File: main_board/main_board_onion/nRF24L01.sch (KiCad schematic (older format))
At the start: 20 parts, among them Q8 BSS138, U10 nRF24L01P, U11 molex_antenna_47948-0001, U9 Trinket_M0, Y2 16Mhz

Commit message: Forgot to save before last commit
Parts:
- removed Q8: BSS138, Package_TO_SOT_SMD:SOT-23, symbol Transistor_FET:BSS138
- removed U9: Trinket_M0, Trinket:Trinket_M0_noMounting, symbol Trinket:Trinket_M0
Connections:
- net labels removed: 5V, Trinket_RST
- wire segments 88 -> 75
- no-connect marks 5 -> 4
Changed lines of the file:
@@
 $Descr A4 11693 8268
 encoding utf-8
-Sheet 6 6
+Sheet 6 7
 Title ""
 Date ""
@@
 Wire Wire Line
 	7525 2050 7425 2050
-Text HLabel 2075 3725 0    50   Input ~ 0
-5V
 Connection ~ 6075 1100
 Wire Wire Line
@@
 Text Label 6525 775  2    50   ~ 0
 3v3_Trinket
-$Comp
-L Trinket:Trinket_M0 U9
-U 1 1 5D093872
-P 3075 3925
-AR Path="/5D093872" Ref="U9"  Part="1"
-AR Path="/5D07F3D0/5D093872" Ref="U9"  Part="1"
-F 0 "U9" H 3025 4390 50  0000 C CNN
-F 1 "Trinket_M0" H 3025 4299 50  0000 C CNN
-F 2 "Trinket:Trinket_M0_noMounting" H 3025 4025 50  0001 C CNN
-F 3 "https://learn.adafruit.com/adafruit-trinket-m0-circuitpython-arduino/downloads" H 3025 4025 50  0001 C CNN
-	1    3075 3925
-	1    0    0    -1
-$EndComp
-NoConn ~ 3775 3725
-$Comp
-L Transistor_FET:BSS138 Q8
-U 1 1 5D099668
-P 1975 4525
-F 0 "Q8" V 2226 4525 50  0000 C CNN
-F 1 "BSS138" V 2317 4525 50  0000 C CNN
-F 2 "Package_TO_SOT_SMD:SOT-23" H 2175 4450 50  0001 L CIN
-F 3 "https://www.fairchildsemi.com/datasheets/BS/BSS138.pdf" H 1975 4525 50  0001 L CNN
-	1    1975 4525
-	1    0    0    -1
-$EndComp
-Wire Wire Line
-	2275 4125 2075 4125
-Wire Wire Line
-	2075 4125 2075 4325
-Wire Wire Line
-	2075 4725 2075 4875
-Wire Wire Line
-	2075 4875 2275 4875
-Text Label 2275 4875 2    50   ~ 0
-GND
-Text Label 1750 4525 2    50   ~ 0
-Trinket_RST
-Wire Wire Line
-	1775 4525 1325 4525
-Text HLabel 1325 4525 0    50   Input ~ 0
-Trinket_RST
-Text Label 2100 3825 0    50   ~ 0
-GND
-Wire Wire Line
-	2100 3825 2275 3825
-Text Label 4250 4125 2    50   ~ 0
-3v3_Trinket
 NoConn ~ 6825 3000
 Text Label 6775 2900 2    50   ~ 0
 nRF_CE
-Text Label 1900 4025 0    50   ~ 0
-nRF_SCK
-Text Label 4125 3925 2    50   ~ 0
-nRF_CSN
-Text Label 4075 3825 2    50   ~ 0
-nRF_CE
-Text Label 1875 3925 0    50   ~ 0
-nRF_MOSI
-Text Label 4175 4025 2    50   ~ 0
-nRF_MISO
 Wire Wire Line
 	6400 2500 6825 2500
@@
 	6400 2900 6825 2900
 Wire Wire Line
-	3775 3925 4125 3925
-Wire Wire Line
-	3775 3825 4075 3825
-Wire Wire Line
-	2275 3925 1875 3925
-Wire Wire Line
-	3775 4025 4175 4025
-Wire Wire Line
-	2275 4025 1900 4025
-Wire Wire Line
-	2075 3725 2275 3725
-Wire Wire Line
-	3775 4125 4250 4125
-Wire Wire Line
 	6075 775  6525 775
 Wire Wire Line
 	6775 2050 7325 2050
+$Sheet
+S 2975 3225 1900 1400
+U 5D0BDDAB
+F0 "Trinket_M0_rev_D" 50
+F1 "/home/jonathan/Projects/SB_CAD/SUPERball/superball_v2_electronics/Adafruit-Trinket-M0-PCB-master/Trinket M0 rev D/Trinket_M0_rev_D.sch" 50
+$EndSheet
 $EndSCHEMATC

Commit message: pulled updated sch files from dev_nRF24 branch. Need to get new nRF24 lib from same branch.
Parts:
- removed C33: 1nF, Capacitor_SMD:C_0603_1608Metric, symbol Device:C_Small
- U10: symbol RF:nRF24L01P -> New_nRF24:nRF24L01P
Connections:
- net labels added: 3v3, Trinket_RESET
- wire segments 75 -> 84
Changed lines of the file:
@@
 EESchema Schematic File Version 5
-LIBS:main_board_onion-cache
+LIBS:nRF24_testing-cache
 EELAYER 29 0
 EELAYER END
 $Descr A4 11693 8268
 encoding utf-8
-Sheet 6 7
+Sheet 2 3
 Title ""
 Date ""
@@
 Wire Wire Line
 	6075 825  6075 775
-Connection ~ 7425 3775
 Wire Wire Line
 	5900 775  6075 775
@@
 	1    0    0    -1
 $EndComp
-Text Label 6775 2700 2    50   ~ 0
-nRF_CSN
 Wire Wire Line
 	8325 3850 8275 3850
@@
 Wire Wire Line
 	8275 3500 8275 3850
-Wire Wire Line
-	5900 1100 5800 1100
 Text Label 8650 3675 2    50   ~ 0
 GND
 Wire Wire Line
 	8275 3400 8275 3500
-Text Label 7050 3775 0    50   ~ 0
-GND
 Wire Wire Line
 	5900 1025 5900 1100
@@
 	9475 2150 9475 2025
 Connection ~ 7325 2050
-Connection ~ 7325 3775
 Connection ~ 6075 775
 Text HLabel 6400 2600 0    50   Input ~ 0
@@
 Wire Wire Line
 	7425 2100 7425 2050
-Connection ~ 5900 1100
 Wire Wire Line
 	6075 1025 6075 1100
@@
 Text Label 6250 1100 2    50   ~ 0
 GND
-$Comp
-L Device:C_Small C33
-U 1 1 5D08136B
-P 6075 925
-F 0 "C33" H 6167 971 50  0000 L CNN
-F 1 "1nF" H 6167 880 50  0000 L CNN
-F 2 "Capacitor_SMD:C_0603_1608Metric" H 6075 925 50  0001 C CNN
-F 3 "~" H 6075 925 50  0001 C CNN
-	1    6075 925
-	1    0    0    -1
-$EndComp
 Wire Wire Line
 	5900 825  5900 775
-Text HLabel 5800 1100 0    50   Input ~ 0
+Text HLabel 1750 3900 0    50   Input ~ 0
 GND
 Wire Wire Line
@@
 Text Label 6775 2400 2    50   ~ 0
 nRF_MOSI
-Wire Wire Line
-	7425 3775 7325 3775
 Text HLabel 6400 2500 0    50   Input ~ 0
 nRF_MISO
 $Comp
-L RF:nRF24L01P U10
+L New_nRF24:nRF24L01P U10
 U 1 1 5D07F55C
 P 7425 2900
@@
 	0    -1   -1   0
 $EndComp
-Text Label 7050 3775 0    50   ~ 0
+Text Label 6975 3775 0    50   ~ 0
 GND
 Wire Wire Line
@@
 Text Label 8650 3350 2    50   ~ 0
 GND
-$Comp
-L Device:C_Small C37
-U 1 1 5D095A49
-P 8675 4075
-F 0 "C37" H 8767 4121 50  0000 L CNN
-F 1 "12pF" H 8767 4030 50  0000 L CNN
-F 2 "Capacitor_SMD:C_0603_1608Metric" H 8675 4075 50  0001 C CNN
-F 3 "~" H 8675 4075 50  0001 C CNN
-	1    8675 4075
-	1    0    0    -1
-$EndComp
 Wire Wire Line
 	9525 2825 10225 2825
@@
 $EndComp
 Wire Wire Line
-	6725 3775 7325 3775
+	6725 3775 7225 3775
 Connection ~ 8300 2600
 NoConn ~ 10925 2725
@@
 	6400 2600 6825 2600
 Wire Wire Line
-	6400 2700 6825 2700
-Wire Wire Line
 	6400 2900 6825 2900
 Wire Wire Line
@@
 	6775 2050 7325 2050
 $Sheet
-S 2975 3225 1900 1400
+S 1975 3550 1900 1400
 U 5D0BDDAB
 F0 "Trinket_M0_rev_D" 50
 F1 "/home/jonathan/Projects/SB_CAD/SUPERball/superball_v2_electronics/Adafruit-Trinket-M0-PCB-master/Trinket M0 rev D/Trinket_M0_rev_D.sch" 50
+F2 "3v3" I L 1975 3800 50
+F3 "GND" I L 1975 3900 50
+F4 "~RESET_M0" I L 1975 4200 50
+F5 "MISO" I R 3875 3775 50
+F6 "SCK" I R 3875 3875 50
+F7 "MOSI" I R 3875 3675 50
+F8 "D0{slash}CE" I R 3875 4175 50
+F9 "D1{slash}CSN" I R 3875 3975 50
 $EndSheet
+Text Label 6775 2700 2    50   ~ 0
+nRF_CSN
+Wire Wire Line
+	6400 2700 6825 2700
+Wire Wire Line
+	3875 3675 4300 3675
+Text Label 4250 3875 2    50   ~ 0
+nRF_SCK
+Text Label 4250 3775 2    50   ~ 0
+nRF_MISO
+Text Label 4250 4175 2    50   ~ 0
+nRF_CE
+Wire Wire Line
+	3875 4175 4300 4175
+Text Label 4250 3975 2    50   ~ 0
+nRF_CSN
+Wire Wire Line
+	3875 3775 4300 3775
+Wire Wire Line
+	3875 3975 4250 3975
+Text Label 4250 3675 2    50   ~ 0
+nRF_MOSI
+Wire Wire Line
+	3875 3875 4300 3875
+Text Label 1750 3900 0    50   ~ 0
+GND
+Wire Wire Line
+	1975 3900 1750 3900
+Text Label 1500 3800 0    50   ~ 0
+3v3_Trinket
+Wire Wire Line
+	1975 3800 1500 3800
+Wire Wire Line
+	1975 4200 1625 4200
+Text HLabel 1625 4200 0    50   Input ~ 0
+Trinket_RESET
+Text HLabel 1500 3800 0    50   Input ~ 0
+3v3
+$Comp
+L Device:C_Small C37
+U 1 1 5D095A49
+P 8675 4075
+F 0 "C37" H 8767 4121 50  0000 L CNN
+F 1 "12pF" H 8767 4030 50  0000 L CNN
+F 2 "Capacitor_SMD:C_0603_1608Metric" H 8675 4075 50  0001 C CNN
+F 3 "~" H 8675 4075 50  0001 C CNN
+	1    8675 4075
+	1    0    0    -1
+$EndComp
+Connection ~ 7325 3775
+Connection ~ 7425 3775
+Wire Wire Line
+	7425 3775 7325 3775
+Wire Wire Line
+	7225 3700 7225 3775
+Connection ~ 7225 3775
+Wire Wire Line
+	7225 3775 7325 3775
 $EndSCHEMATC

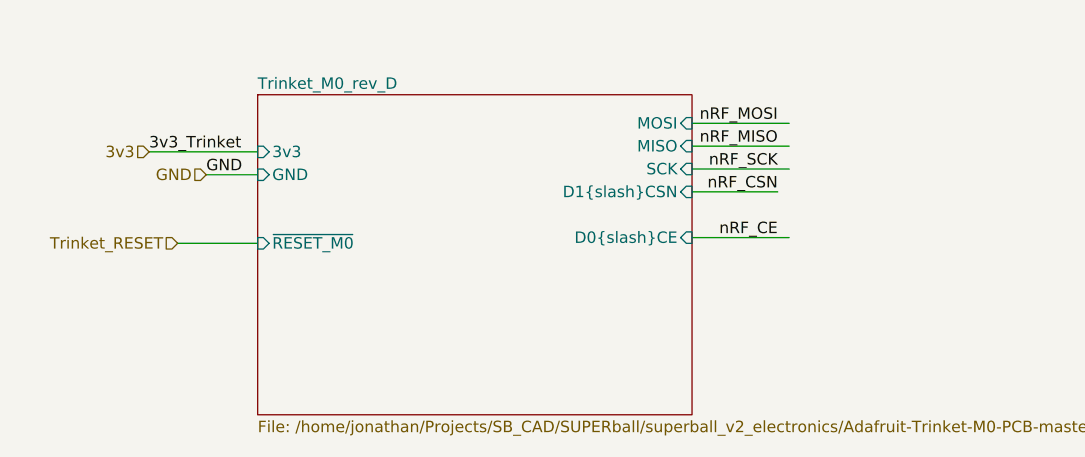
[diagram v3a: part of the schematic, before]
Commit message: Added new nRF24 library
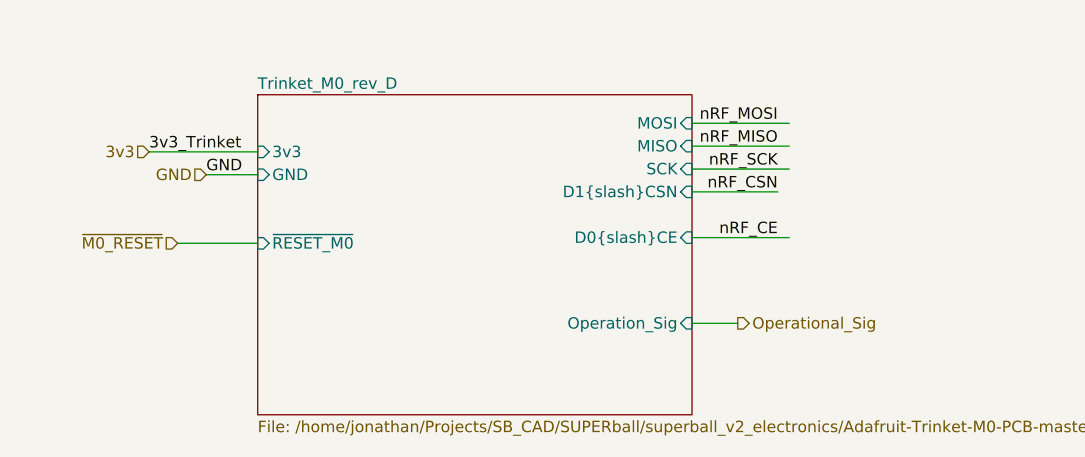
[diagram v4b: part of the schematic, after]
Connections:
- net labels added: Operational_Sig, ~M0_RESET
- net labels removed: Trinket_RESET
- wire segments 84 -> 85
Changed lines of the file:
@@
 EESchema Schematic File Version 5
-LIBS:nRF24_testing-cache
+LIBS:main_board_onion-cache
 EELAYER 29 0
 EELAYER END
 $Descr A4 11693 8268
 encoding utf-8
-Sheet 2 3
+Sheet 6 7
 Title ""
 Date ""
@@
 F8 "D0{slash}CE" I R 3875 4175 50
 F9 "D1{slash}CSN" I R 3875 3975 50
+F10 "Operation_Sig" I R 3875 4550 50
 $EndSheet
 Text Label 6775 2700 2    50   ~ 0
@@
 	1975 4200 1625 4200
 Text HLabel 1625 4200 0    50   Input ~ 0
-Trinket_RESET
+~M0_RESET
 Text HLabel 1500 3800 0    50   Input ~ 0
 3v3
@@
 Wire Wire Line
 	7225 3775 7325 3775
+Text HLabel 4075 4550 2    50   Output ~ 0
+Operational_Sig
+Wire Wire Line
+	3875 4550 4075 4550
 $EndSCHEMATC

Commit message: Finished initial routing of this design
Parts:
- C32, C34, C35, C36, C37, C38, C39, C40, C41: footprint Capacitor_SMD:C_0603_1608Metric -> Capacitor_SMD:C_0402_1005Metric
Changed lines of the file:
@@
 $Descr A4 11693 8268
 encoding utf-8
-Sheet 6 7
+Sheet 5 7
 Title ""
 Date ""
@@
 F 0 "C34" H 6167 971 50  0000 L CNN
 F 1 "1nF" H 6167 880 50  0000 L CNN
-F 2 "Capacitor_SMD:C_0603_1608Metric" H 6075 925 50  0001 C CNN
+F 2 "Capacitor_SMD:C_0402_1005Metric" H 6075 925 50  0001 C CNN
 F 3 "~" H 6075 925 50  0001 C CNN
 	1    6075 925
@@
 F 0 "C32" H 5700 1000 50  0000 L CNN
 F 1 "10nF" H 5650 875 50  0000 L CNN
-F 2 "Capacitor_SMD:C_0603_1608Metric" H 5900 925 50  0001 C CNN
+F 2 "Capacitor_SMD:C_0402_1005Metric" H 5900 925 50  0001 C CNN
 F 3 "~" H 5900 925 50  0001 C CNN
 	1    5900 925
@@
 F 0 "C36" H 8367 4121 50  0000 L CNN
 F 1 "12pF" H 8367 4030 50  0000 L CNN
-F 2 "Capacitor_SMD:C_0603_1608Metric" H 8275 4075 50  0001 C CNN
+F 2 "Capacitor_SMD:C_0402_1005Metric" H 8275 4075 50  0001 C CNN
 F 3 "~" H 8275 4075 50  0001 C CNN
 	1    8275 4075
@@
 F 0 "C35" H 6817 3646 50  0000 L CNN
 F 1 "33nF" H 6817 3555 50  0000 L CNN
-F 2 "Capacitor_SMD:C_0603_1608Metric" H 6725 3600 50  0001 C CNN
+F 2 "Capacitor_SMD:C_0402_1005Metric" H 6725 3600 50  0001 C CNN
 F 3 "~" H 6725 3600 50  0001 C CNN
 	1    6725 3600
@@
 F 0 "C40" V 9246 2250 50  0000 C CNN
 F 1 "4.7pF" V 9337 2250 50  0000 C CNN
-F 2 "Capacitor_SMD:C_0603_1608Metric" H 9475 2250 50  0001 C CNN
+F 2 "Capacitor_SMD:C_0402_1005Metric" H 9475 2250 50  0001 C CNN
 F 3 "~" H 9475 2250 50  0001 C CNN
 	1    9475 2250
@@
 F 0 "C39" V 8946 2825 50  0000 C CNN
 F 1 "1.5pF" V 9037 2825 50  0000 C CNN
-F 2 "Capacitor_SMD:C_0603_1608Metric" H 9175 2825 50  0001 C CNN
+F 2 "Capacitor_SMD:C_0402_1005Metric" H 9175 2825 50  0001 C CNN
 F 3 "~" H 9175 2825 50  0001 C CNN
 	1    9175 2825
@@
 Wire Wire Line
 	8025 2400 9125 2400
-$Comp
-L Device:C_Small C38
-U 1 1 5D0A7690
-P 9125 2250
-F 0 "C38" V 8896 2250 50  0000 C CNN
-F 1 "2.2nF" V 8987 2250 50  0000 C CNN
-F 2 "Capacitor_SMD:C_0603_1608Metric" H 9125 2250 50  0001 C CNN
-F 3 "~" H 9125 2250 50  0001 C CNN
-	1    9125 2250
-	-1   0    0    1
-$EndComp
 Wire Wire Line
 	8900 2825 9075 2825
@@
 F 0 "C41" V 9296 2950 50  0000 C CNN
 F 1 "1.0pF" V 9387 2950 50  0000 C CNN
-F 2 "Capacitor_SMD:C_0603_1608Metric" H 9525 2950 50  0001 C CNN
+F 2 "Capacitor_SMD:C_0402_1005Metric" H 9525 2950 50  0001 C CNN
 F 3 "~" H 9525 2950 50  0001 C CNN
 	1    9525 2950
@@
 F 0 "C37" H 8767 4121 50  0000 L CNN
 F 1 "12pF" H 8767 4030 50  0000 L CNN
-F 2 "Capacitor_SMD:C_0603_1608Metric" H 8675 4075 50  0001 C CNN
+F 2 "Capacitor_SMD:C_0402_1005Metric" H 8675 4075 50  0001 C CNN
 F 3 "~" H 8675 4075 50  0001 C CNN
 	1    8675 4075
@@
 Wire Wire Line
 	3875 4550 4075 4550
+$Comp
+L Device:C_Small C38
+U 1 1 5D0A7690
+P 9125 2250
+F 0 "C38" V 8896 2250 50  0000 C CNN
+F 1 "2.2nF" V 8987 2250 50  0000 C CNN
+F 2 "Capacitor_SMD:C_0402_1005Metric" H 9125 2250 50  0001 C CNN
+F 3 "~" H 9125 2250 50  0001 C CNN
+	1    9125 2250
+	-1   0    0    1
+$EndComp
 $EndSCHEMATC

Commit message: Added Gerber files for the version uploaded to MacroFab for manufacturing. Plus small changes made before uploading it.
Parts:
- Y2: value 16Mhz -> CX3225SB16000H0FLJCC
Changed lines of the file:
@@
 P 8475 3500
 F 0 "Y2" H 8331 3454 50  0000 R CNN
-F 1 "16Mhz" H 8331 3545 50  0000 R CNN
+F 1 " CX3225SB16000H0FLJCC " H 8331 3545 50  0000 R CNN
 F 2 "Crystal:Crystal_SMD_3225-4Pin_3.2x2.5mm" H 8475 3500 50  0001 C CNN
 F 3 "https://media.digikey.com/pdf/Data%20Sheets/AVX%20PDFs/CX3225SB_UKY1C-H1-16357-00_Spec.pdf" H 8475 3500 50  0001 C CNN
